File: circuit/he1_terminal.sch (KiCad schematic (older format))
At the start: 4 parts, among them J1 DB25, Q1 Q_NPN_CBE, U1 LTV-817

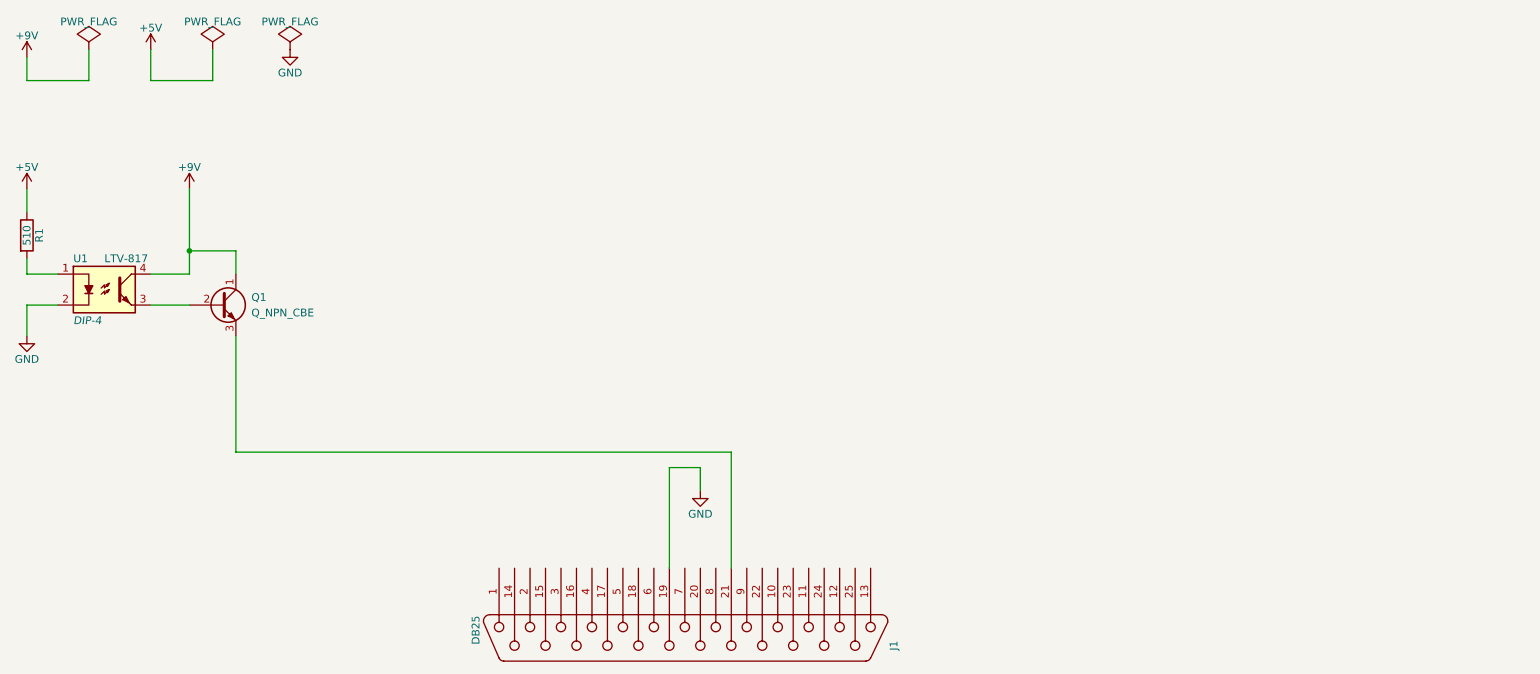
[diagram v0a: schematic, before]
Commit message: add leds to schematics
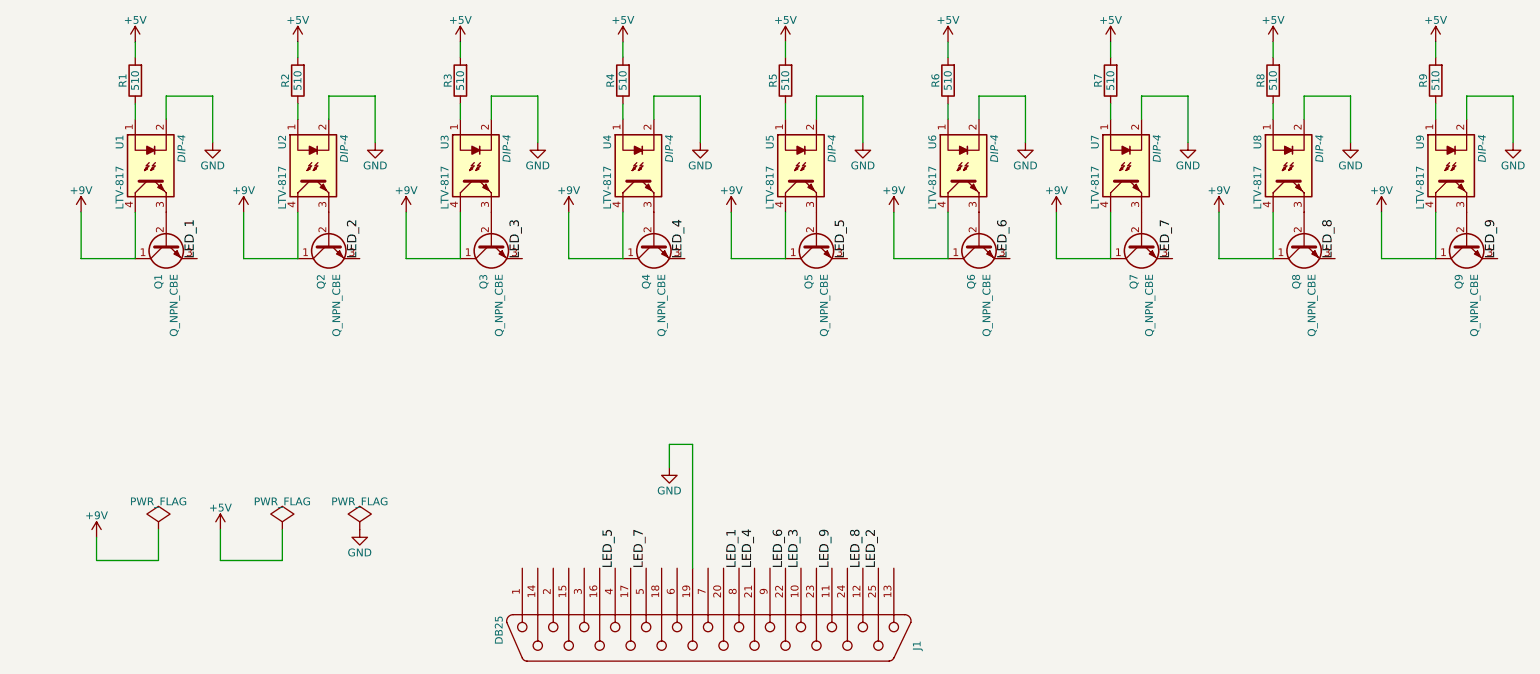
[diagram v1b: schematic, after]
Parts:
- added Q2, Q3, Q4, Q5, Q6, Q7, Q8, Q9: Q_NPN_CBE, symbol Q_NPN_CBE
- added R2, R3, R4, R5, R6, R7, R8, R9: 510, symbol R
- added U2, U3, U4, U5, U6, U7, U8, U9: LTV-817, DIP-4, symbol LTV-817
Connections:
- net +5V: now also R1.2, R2.2, R3.2, R4.2, R5.2, R6.2, R7.2, R8.2, R9.2; no longer R1.1
- net +9V: now also Q2.1 (C), Q3.1 (C), Q4.1 (C), Q5.1 (C), Q6.1 (C), Q7.1 (C), Q8.1 (C), Q9.1 (C), U2.4, U3.4, U4.4, U5.4, U6.4, U7.4, U8.4, U9.4
- net GND: now also U2.2, U3.2, U4.2, U5.2, U6.2, U7.2, U8.2, U9.2
- net LED_1: now reaches Q1.3 (E)
- net LED_1: now also J1.8; no longer J1.21 (P21)
- net LED_3: now reaches J1.10
- net LED_3: now also Q3.3 (E)
- net LED_9: now reaches J1.11
- net LED_9: now also Q9.3 (E)
- net LED_8: now reaches J1.12
- net LED_8: now also Q8.3 (E)
- net LED_6: now reaches J1.22 (P22)
- net LED_6: now also Q6.3 (E)
- net LED_2: now reaches J1.25 (P25)
- net LED_2: now also Q2.3 (E)
- net LED_5: now reaches J1.4
- net LED_5: now also Q5.3 (E)
- net LED_7: now reaches J1.5
- net LED_7: now also Q7.3 (E)
- net at U1.1: now also R1.1; no longer R1.2
- new net: Q2.2 (B), U2.3
- new net: R2.1, U2.1
- new net: Q3.2 (B), U3.3
- new net: R3.1, U3.1
- new net: Q4.2 (B), U4.3
- new net: R4.1, U4.1
- new net: Q5.2 (B), U5.3
- new net: R5.1, U5.1
- new net: Q6.2 (B), U6.3
- new net: R6.1, U6.1
- new net: Q7.2 (B), U7.3
- new net: R7.1, U7.1
- new net: Q8.2 (B), U8.3
- new net: R8.1, U8.1
- new net: Q9.2 (B), U9.3
- new net: R9.1, U9.1
- new net LED_4: J1.21 (P21), Q4.3 (E)
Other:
- moved on the sheet: J1

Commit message: migrate to current kicad version
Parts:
- J1: symbol DB25 -> he1_terminal-rescue:DB25
- Q1, Q2, Q3, Q4, Q5, Q6, Q7, Q8, Q9: symbol Q_NPN_CBE -> he1_terminal-rescue:Q_NPN_CBE
- R1, R2, R3, R4, R5, R6, R7, R8, R9: symbol R -> he1_terminal-rescue:R
- U1, U2, U3, U4, U5, U6, U7, U8, U9: symbol LTV-817 -> he1_terminal-rescue:LTV-817
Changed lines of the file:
@@
-EESchema Schematic File Version 2
-LIBS:power
-LIBS:device
-LIBS:transistors
-LIBS:conn
-LIBS:linear
-LIBS:regul
-LIBS:74xx
-LIBS:cmos4000
-LIBS:adc-dac
-LIBS:memory
-LIBS:xilinx
-LIBS:microcontrollers
-LIBS:dsp
-LIBS:microchip
-LIBS:analog_switches
-LIBS:motorola
-LIBS:texas
-LIBS:intel
-LIBS:audio
-LIBS:interface
-LIBS:digital-audio
-LIBS:philips
-LIBS:display
-LIBS:cypress
-LIBS:siliconi
-LIBS:opto
-LIBS:atmel
-LIBS:contrib
-LIBS:valves
+EESchema Schematic File Version 4
 LIBS:he1_terminal-cache
-EELAYER 25 0
+EELAYER 26 0
 EELAYER END
 $Descr A4 11693 8268
@@
 $EndDescr
 $Comp
-L +9V #PWR2
+L power:+9V #PWR2
 U 1 1 58D791F1
 P 1200 4050
@@
 $EndComp
 $Comp
-L +5V #PWR5
+L power:+5V #PWR5
 U 1 1 58D79227
 P 2000 4000
@@
 $EndComp
 $Comp
-L GND #PWR8
+L power:GND #PWR8
 U 1 1 58D792C3
 P 2900 4000
@@
 $EndComp
 $Comp
-L PWR_FLAG #FLG3
+L power:PWR_FLAG #FLG3
 U 1 1 58D79607
 P 2900 4000
@@
 $EndComp
 $Comp
-L PWR_FLAG #FLG1
+L power:PWR_FLAG #FLG1
 U 1 1 58D7963B
 P 1600 4000
@@
 $EndComp
 $Comp
-L PWR_FLAG #FLG2
+L power:PWR_FLAG #FLG2
 U 1 1 58D7966D
 P 2400 4000
@@
 $EndComp
 $Comp
-L DB25 J1
+L he1_terminal-rescue:DB25 J1
 U 1 1 58D79A54
 P 5150 4700
@@
 $EndComp
 $Comp
-L GND #PWR15
+L power:GND #PWR15
 U 1 1 58D7A1BB
 P 4900 3600
@@
 	2400 4200 2400 4000
 $Comp
-L Q_NPN_CBE Q1
+L he1_terminal-rescue:Q_NPN_CBE Q1
 U 1 1 58E3F007
 P 1650 2150
@@
 $EndComp
 $Comp
-L +9V #PWR1
+L power:+9V #PWR1
 U 1 1 58E3F00D
 P 1100 1950
@@
 $EndComp
 $Comp
-L R R1
+L he1_terminal-rescue:R R1
 U 1 1 58E3F013
 P 1450 1100
@@
 $EndComp
 $Comp
-L +5V #PWR3
+L power:+5V #PWR3
 U 1 1 58E3F019
 P 1450 850
@@
 $EndComp
 $Comp
-L GND #PWR4
+L power:GND #PWR4
 U 1 1 58E3F01F
 P 1950 1500
@@
 $EndComp
 $Comp
-L LTV-817 U1
+L he1_terminal-rescue:LTV-817 U1
 U 1 1 58E3F025
 P 1550 1650
@@
 	1450 950  1450 850
 $Comp
-L Q_NPN_CBE Q2
+L he1_terminal-rescue:Q_NPN_CBE Q2
 U 1 1 58E3FDD3
 P 2700 2150
@@
 $EndComp
 $Comp
-L +9V #PWR6
+L power:+9V #PWR6
 U 1 1 58E3FDD9
 P 2150 1950
@@
 $EndComp
 $Comp
-L R R2
+L he1_terminal-rescue:R R2
 U 1 1 58E3FDDF
 P 2500 1100
@@
 $EndComp
 $Comp
-L +5V #PWR7
+L power:+5V #PWR7
 U 1 1 58E3FDE5
 P 2500 850
@@
 $EndComp
 $Comp
-L GND #PWR9
+L power:GND #PWR9
 U 1 1 58E3FDEB
 P 3000 1500
@@
 $EndComp
 $Comp
-L LTV-817 U2
+L he1_terminal-rescue:LTV-817 U2
 U 1 1 58E3FDF1
 P 2600 1650
@@
 	2500 950  2500 850
 $Comp
-L Q_NPN_CBE Q3
+L he1_terminal-rescue:Q_NPN_CBE Q3
 U 1 1 58E400BF
 P 3750 2150
@@
 $EndComp
 $Comp
-L +9V #PWR10
+L power:+9V #PWR10
 U 1 1 58E400C5
 P 3200 1950
@@
 $EndComp
 $Comp
-L R R3
+L he1_terminal-rescue:R R3
 U 1 1 58E400CB
 P 3550 1100
@@
 $EndComp
 $Comp
-L +5V #PWR11
+L power:+5V #PWR11
 U 1 1 58E400D1
 P 3550 850
@@
 $EndComp
 $Comp
-L GND #PWR12
+L power:GND #PWR12
 U 1 1 58E400D7
 P 4050 1500
@@
 $EndComp
 $Comp
-L LTV-817 U3
+L he1_terminal-rescue:LTV-817 U3
 U 1 1 58E400DD
 P 3650 1650
@@
 	3550 950  3550 850
 $Comp
-L Q_NPN_CBE Q4
+L he1_terminal-rescue:Q_NPN_CBE Q4
 U 1 1 58E40487
 P 4800 2150
@@
 $EndComp
 $Comp
-L +9V #PWR13
+L power:+9V #PWR13
 U 1 1 58E4048D
 P 4250 1950
@@
 $EndComp
 $Comp
-L R R4
+L he1_terminal-rescue:R R4
 U 1 1 58E40493
 P 4600 1100
@@
 $EndComp
 $Comp
-L +5V #PWR14
+L power:+5V #PWR14
 U 1 1 58E40499
 P 4600 850
@@
 $EndComp
 $Comp
-L GND #PWR16
+L power:GND #PWR16
 U 1 1 58E4049F
 P 5100 1500
@@
 $EndComp
 $Comp
-L LTV-817 U4
+L he1_terminal-rescue:LTV-817 U4
 U 1 1 58E404A5
 P 4700 1650
@@
 	4600 950  4600 850
 $Comp
-L Q_NPN_CBE Q5
+L he1_terminal-rescue:Q_NPN_CBE Q5
 U 1 1 58E40F46
 P 5850 2150
@@
 $EndComp
 $Comp
-L +9V #PWR17
+L power:+9V #PWR17
 U 1 1 58E40F4C
 P 5300 1950
@@
 $EndComp
 $Comp
-L R R5
+L he1_terminal-rescue:R R5
 U 1 1 58E40F52
 P 5650 1100
@@
 $EndComp
 $Comp
-L +5V #PWR18
+L power:+5V #PWR18
 U 1 1 58E40F58
 P 5650 850
@@
 $EndComp
 $Comp
-L GND #PWR19
+L power:GND #PWR19
 U 1 1 58E40F5E
 P 6150 1500
@@
 $EndComp
 $Comp
-L LTV-817 U5
+L he1_terminal-rescue:LTV-817 U5
 U 1 1 58E40F64
 P 5750 1650
@@
 	5650 950  5650 850
 $Comp
-L Q_NPN_CBE Q6
+L he1_terminal-rescue:Q_NPN_CBE Q6
 U 1 1 58E4118F
 P 6900 2150
@@
 $EndComp
 $Comp
-L +9V #PWR20
+L power:+9V #PWR20
 U 1 1 58E41195
 P 6350 1950
@@
 $EndComp
 $Comp
-L R R6
+L he1_terminal-rescue:R R6
 U 1 1 58E4119B
 P 6700 1100
@@
 $EndComp
 $Comp
-L +5V #PWR21
+L power:+5V #PWR21
 U 1 1 58E411A1
 P 6700 850
@@
 $EndComp
 $Comp
-L GND #PWR22
+L power:GND #PWR22
 U 1 1 58E411A7
 P 7200 1500
@@
 $EndComp
 $Comp
-L LTV-817 U6
+L he1_terminal-rescue:LTV-817 U6
 U 1 1 58E411AD
 P 6800 1650
@@
 	6700 950  6700 850
 $Comp
-L Q_NPN_CBE Q7
+L he1_terminal-rescue:Q_NPN_CBE Q7
 U 1 1 58E4201E
 P 7950 2150
@@
 $EndComp
 $Comp
-L +9V #PWR23
+L power:+9V #PWR23
 U 1 1 58E42024
 P 7400 1950
@@
 $EndComp
 $Comp
-L R R7
+L he1_terminal-rescue:R R7
 U 1 1 58E4202A
 P 7750 1100
@@
 $EndComp
 $Comp
-L +5V #PWR24
+L power:+5V #PWR24
 U 1 1 58E42030
 P 7750 850
@@
 $EndComp
 $Comp
-L GND #PWR25
+L power:GND #PWR25
 U 1 1 58E42036
 P 8250 1500
@@
 $EndComp
 $Comp
-L LTV-817 U7
+L he1_terminal-rescue:LTV-817 U7
 U 1 1 58E4203C
 P 7850 1650
@@
 	7750 950  7750 850
 $Comp
-L Q_NPN_CBE Q8
+L he1_terminal-rescue:Q_NPN_CBE Q8
 U 1 1 58E4350E
 P 9000 2150
@@
 $EndComp
 $Comp
-L +9V #PWR26
+L power:+9V #PWR26
 U 1 1 58E43514
 P 8450 1950
@@
 $EndComp
 $Comp
-L R R8
+L he1_terminal-rescue:R R8
 U 1 1 58E4351A
 P 8800 1100
@@
 $EndComp
 $Comp
-L +5V #PWR27
+L power:+5V #PWR27
 U 1 1 58E43520
 P 8800 850
@@
 $EndComp
 $Comp
-L GND #PWR28
+L power:GND #PWR28
 U 1 1 58E43526
 P 9300 1500
@@
 $EndComp
 $Comp
-L LTV-817 U8
+L he1_terminal-rescue:LTV-817 U8
 U 1 1 58E4352C
 P 8900 1650
@@
 	8800 950  8800 850
 $Comp
-L Q_NPN_CBE Q9
+L he1_terminal-rescue:Q_NPN_CBE Q9
 U 1 1 58E43640
 P 10050 2150
@@
 $EndComp
 $Comp
-L +9V #PWR29
+L power:+9V #PWR29
 U 1 1 58E43646
 P 9500 1950
@@
 $EndComp
 $Comp
-L R R9
+L he1_terminal-rescue:R R9
 U 1 1 58E4364C
 P 9850 1100
@@
 $EndComp
 $Comp
-L +5V #PWR30
+L power:+5V #PWR30
 U 1 1 58E43652
 P 9850 850
@@
 $EndComp
 $Comp
-L GND #PWR31
+L power:GND #PWR31
 U 1 1 58E43658
 P 10350 1500
@@
 $EndComp
 $Comp
-L LTV-817 U9
+L he1_terminal-rescue:LTV-817 U9
 U 1 1 58E4365E
 P 9950 1650
